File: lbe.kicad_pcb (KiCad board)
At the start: 2 copper layers, 95 parts, among them J1 Screw_Terminal_1x03, J2 IN, J3 IN, J4 IN, J5 IN, J6 IN, J7 IN, J8 IN, J9 IN, M1 BLUEPILL_STM8S103F3, U1 SN74LV1T34, U2 74HC245, U3 MCP6004, U4 MCP6004

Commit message: Layout complete
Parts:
- added J10: Screw_Terminal_1x02, Connectors_Phoenix:PhoenixContact_MC-G_02x3.81mm_Angled, F.Cu at (169.5, 62.2)
- added REF**: MountingHole_3.2mm_M3, Mounting_Holes:MountingHole_3.2mm_M3, F.Cu at (173.0, 47.0)
- added REF**: MountingHole_3.2mm_M3, Mounting_Holes:MountingHole_3.2mm_M3, F.Cu at (173.0, 98.0)
- added REF**: MountingHole_3.2mm_M3, Mounting_Holes:MountingHole_3.2mm_M3, F.Cu at (55.0, 98.0)
- added REF**: MountingHole_3.2mm_M3, Mounting_Holes:MountingHole_3.2mm_M3, F.Cu at (55.0, 47.0)
- C10: moved to F.Cu
- C5: footprint Capacitors_SMD:C_0603_HandSoldering -> footprints:Cap_electrolytic_8x10
- C9: moved to B.Cu
- M1: footprint Pin_Headers:Pin_Header_Straight_2x10_Pitch2.54mm -> footprints:BLUEPILL_STM8S103F3
- U2: value 74HC245 -> 74HC245_CUSTOM
- moved U1 56.7 mm to (155.9, 83.2)
- moved J1 56.2 mm to (169.5, 89.2)
- moved C10 54.5 mm to (156.0, 79.2), turned to 180 degrees
- moved C5 47.1 mm to (158.5, 60.8), turned to 90 degrees
- moved D2 46.4 mm to (154.2, 75.0), turned to 90 degrees
- moved C6 46.1 mm to (162.5, 81.5), turned to 180 degrees
- moved L1 46.0 mm to (162.5, 84.5)
- moved M1 45.6 mm to (139.4, 68.6), turned to 180 degrees
- moved R2 42.7 mm to (151.0, 76.5), turned to 270 degrees
- moved C4 42.2 mm to (144.0, 67.2), turned to 270 degrees
- moved D1 40.5 mm to (154.2, 70.0), turned to 270 degrees
- moved R1 35.1 mm to (151.0, 71.5), turned to 270 degrees
- moved C9 32.6 mm to (105.0, 60.0), turned to 270 degrees
- moved C3 30.2 mm to (141.5, 67.2), turned to 270 degrees
- moved C1 30.0 mm to (139.0, 67.2), turned to 270 degrees
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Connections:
- C10 pad 1: VDD -> +5V
- M1 pad 1: /EN1 -> /LED2
- M1 pad 11: /LED2 -> /EN1
- M1 pad 12: /D7 -> /D0
- M1 pad 13: /D6 -> /D1
- M1 pad 14: /D5 -> /D2
- M1 pad 15: /D4 -> /D3
- M1 pad 16: /D3 -> /D4
- M1 pad 17: /D2 -> /D5
- M1 pad 18: /D1 -> /D6
- M1 pad 19: /D0 -> /D7
- U2 pad 20: VCC -> VDD
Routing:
- net GND: track 420.1 -> 702.4 mm, vias 42 -> 90
- net VDD: track 43.0 -> 133.4 mm, vias 2 -> 5
- net +5V: track 0.00 -> 86.5 mm
- net /input_group0/Vref: track 52.6 -> 79.6 mm, vias 0 -> 4
- net /LED_OUT: track 0.00 -> 24.6 mm
- net /THR_PWM: track 0.00 -> 23.0 mm
- net /EN1: track 0.00 -> 9.45 mm
- net Net-(C6-Pad1): track 0.00 -> 9.21 mm
- net /D0: track 0.00 -> 8.55 mm
- net /D7: track 0.00 -> 8.50 mm
- net /LED2: track 0.00 -> 8.04 mm, vias 0 -> 2
- net /D1: track 0.00 -> 8.02 mm
- net /D6: track 0.00 -> 7.97 mm
- net /D2: track 0.00 -> 7.49 mm
- net /D5: track 0.00 -> 7.44 mm
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- added copper zone on B.Cu, net GND
- added copper zone on F.Cu, net GND
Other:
- board outline added: 126 x 59 mm
- net class power added: clearance 0.2, trace_width 2, via_dia 0.6, via_drill 0.4

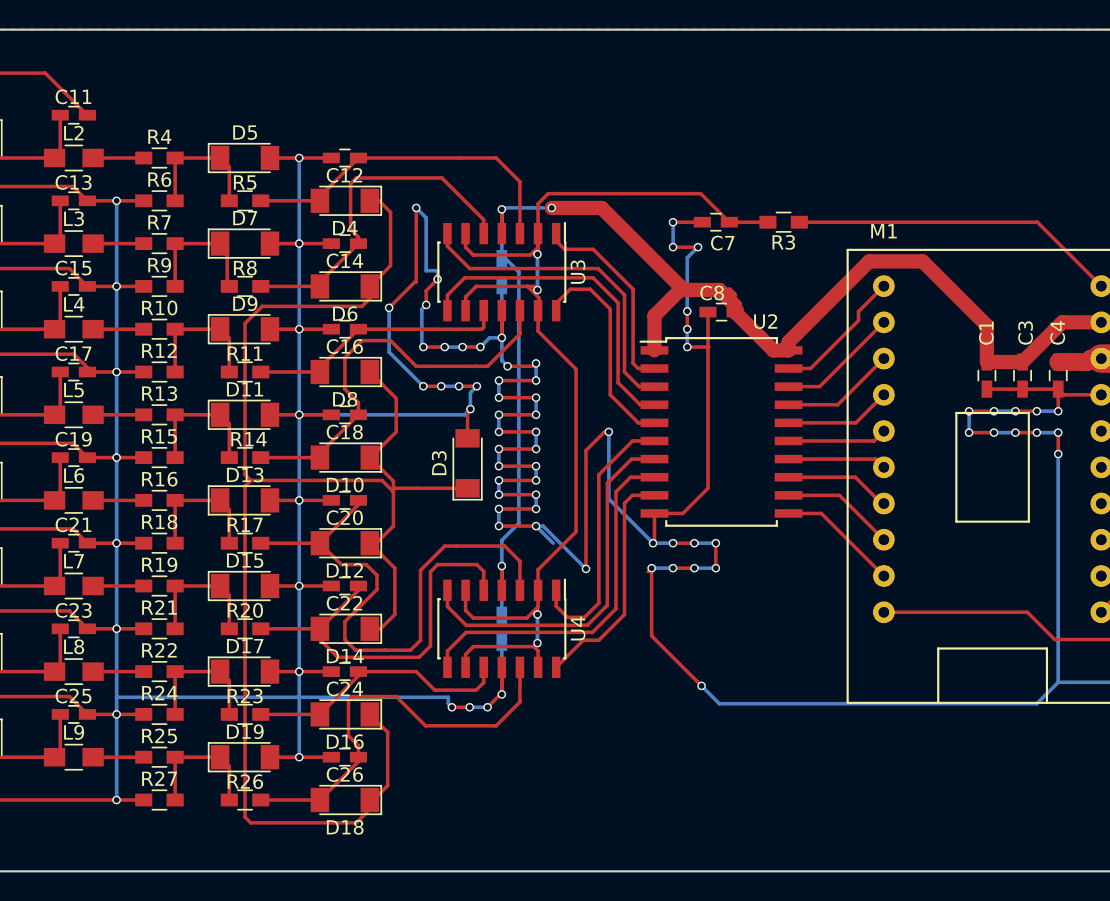
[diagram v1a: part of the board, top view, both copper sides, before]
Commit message: Add pullup option
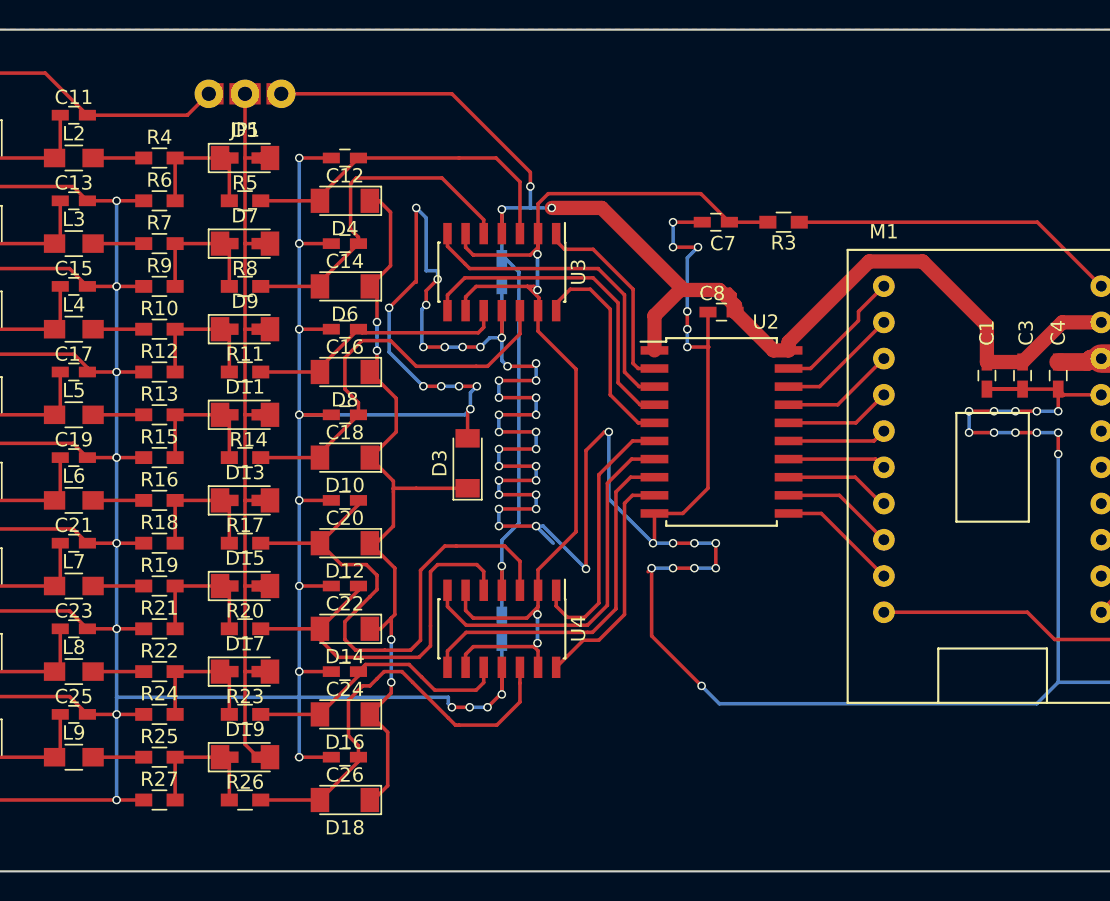
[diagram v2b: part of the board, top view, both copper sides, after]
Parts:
- added JP1: jumper_nc_no_dual, footprints:Header_with_SMD_jumper_1x3_2.54, F.Cu at (87.0, 47.5)
- D11, D13, D15, D17, D19, D5, D7, D9: footprint Diodes_SMD:D_MiniMELF_Standard -> footprints:MiniMelf_0603_combo
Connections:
- D11 pad 2: GND -> /input_group0/sheet5AD30D18/Vclamp
- D13 pad 2: GND -> /input_group0/sheet5AD30D18/Vclamp
- D15 pad 2: GND -> /input_group0/sheet5AD30D18/Vclamp
- D17 pad 2: GND -> /input_group0/sheet5AD30D18/Vclamp
- D19 pad 2: GND -> /input_group0/sheet5AD30D18/Vclamp
- D5 pad 2: GND -> /input_group0/sheet5AD30D18/Vclamp
- D7 pad 2: GND -> /input_group0/sheet5AD30D18/Vclamp
- D9 pad 2: GND -> /input_group0/sheet5AD30D18/Vclamp
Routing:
- net /input_group0/sheet5AD30D18/Vclamp: track 0.00 -> 60.0 mm
- net VCOM: track 109.1 -> 58.0 mm, vias 0 -> 4
- net VDD: track 133.4 -> 156.2 mm, vias 5 -> 6
- net GND: track 702.4 -> 695.3 mm
- net Net-(C26-Pad1): track 28.7 -> 30.1 mm
- net Net-(D7-Pad1): track 9.42 -> 10.3 mm
- net Net-(D9-Pad1): track 9.42 -> 10.1 mm
- net Net-(D19-Pad1): track 9.42 -> 10.1 mm
- net Net-(D17-Pad1): track 9.42 -> 10.1 mm
- net Net-(D15-Pad1): track 9.42 -> 10.1 mm
- net Net-(D13-Pad1): track 9.42 -> 10.1 mm
- net Net-(D11-Pad1): track 9.42 -> 10.1 mm
- net Net-(D5-Pad1): track 9.42 -> 10.1 mm

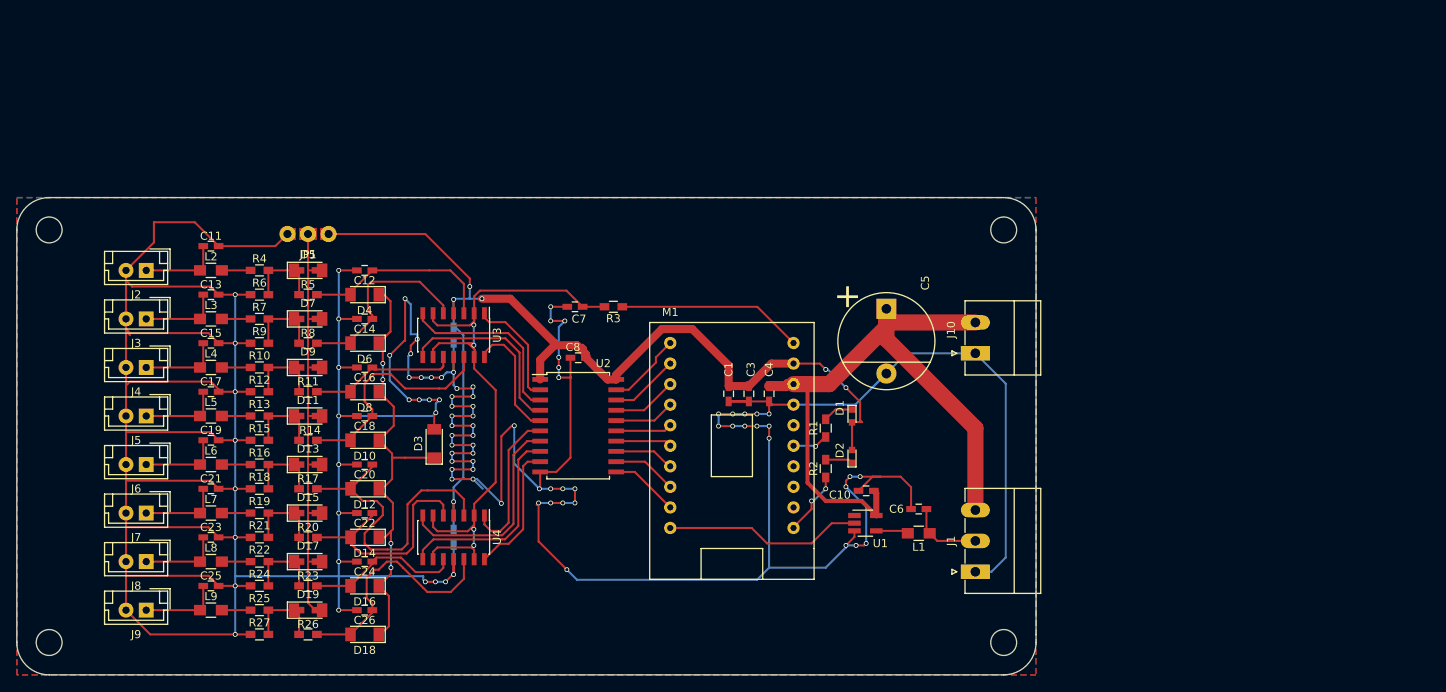
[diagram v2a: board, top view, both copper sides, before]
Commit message: 8ch version without buffer
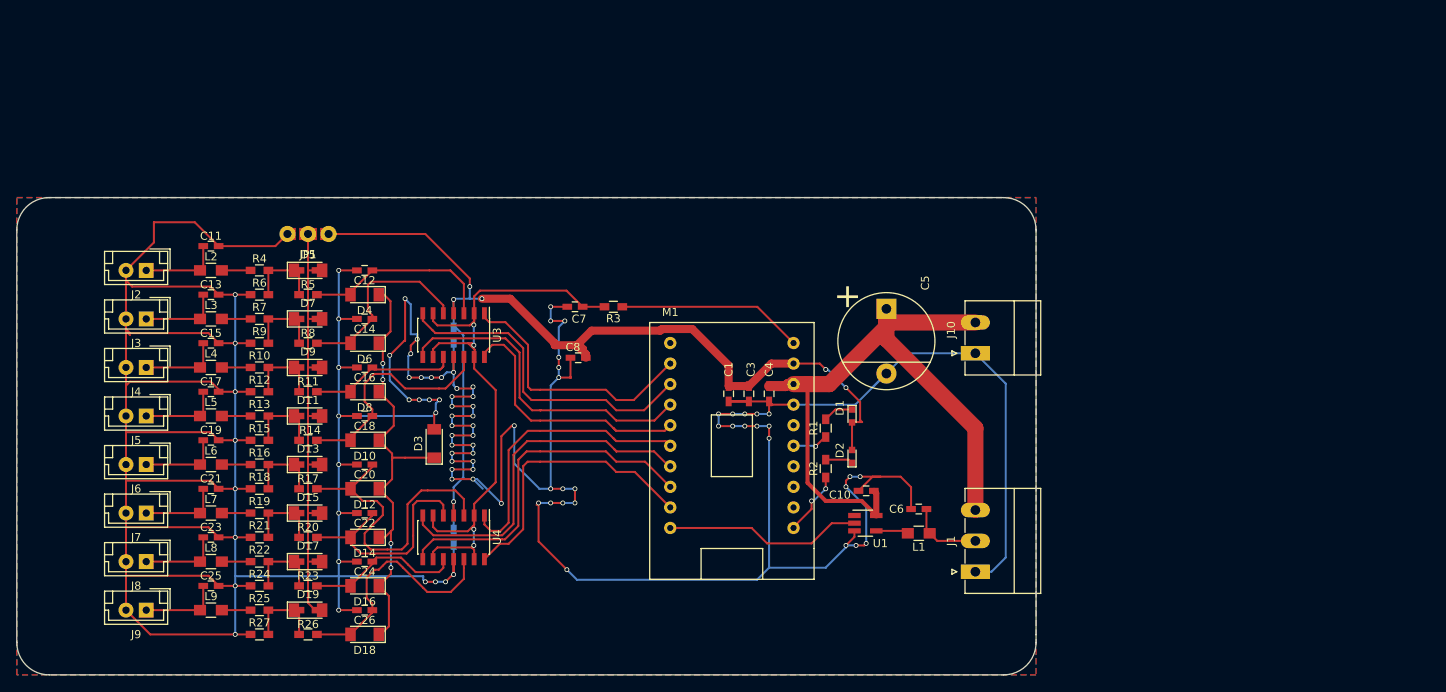
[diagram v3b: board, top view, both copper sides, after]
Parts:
- removed REF** (x4): MountingHole_3.2mm_M3, Mounting_Holes:MountingHole_3.2mm_M3
- removed U2: 74HC245_CUSTOM, Housings_SOIC:SOIC-20W_7.5x12.8mm_Pitch1.27mm
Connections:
- U3 pad 1: /input_group0/sheet5AD30D18/OUT -> /D0
- U3 pad 14: /input_group0/sheet5AD30D1B/OUT -> /D3
- U3 pad 7: /input_group0/sheet5AD30D19/OUT -> /D1
- U3 pad 8: /input_group0/sheet5AD30D1A/OUT -> /D2
- U4 pad 1: /input_group0/sheet5AD30D1C/OUT -> /D4
- U4 pad 14: /input_group0/sheet5AD30D1F/OUT -> /D7
- U4 pad 7: /input_group0/sheet5AD30D1D/OUT -> /D5
- U4 pad 8: /input_group0/sheet5AD30D1E/OUT -> /D6
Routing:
- net /D5: track 7.44 -> 43.6 mm
- net /D6: track 7.97 -> 43.4 mm
- net /D2: track 7.49 -> 40.5 mm
- net /D1: track 8.02 -> 40.6 mm
- net /D4: track 6.92 -> 35.9 mm
- net /D7: track 8.50 -> 34.9 mm
- net /input_group0/sheet5AD30D1D/OUT: track 26.0 -> 0.00 mm
- net /input_group0/sheet5AD30D1E/OUT: track 25.5 -> 0.00 mm
- net /D3: track 6.97 -> 32.4 mm
- net /D0: track 8.55 -> 32.6 mm
- net /input_group0/sheet5AD30D1A/OUT: track 23.1 -> 0.00 mm
- net /input_group0/sheet5AD30D19/OUT: track 22.6 -> 0.00 mm
- net /input_group0/sheet5AD30D1C/OUT: track 18.7 -> 0.00 mm
- net /input_group0/sheet5AD30D1F/OUT: track 16.5 -> 0.00 mm
- net /input_group0/sheet5AD30D1B/OUT: track 15.2 -> 0.00 mm
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
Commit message: Add serial header, restore holes
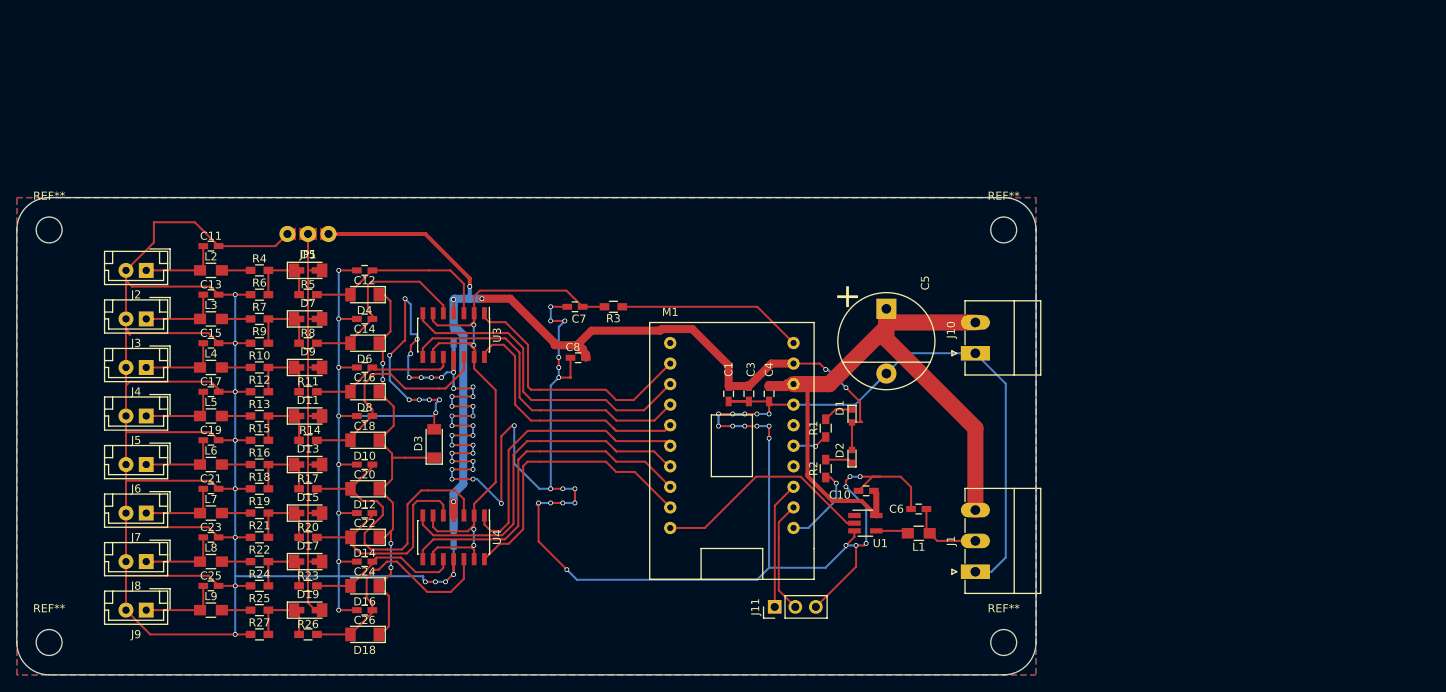
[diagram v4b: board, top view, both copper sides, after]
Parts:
- added J11: CONN_01X03, Pin_Headers:Pin_Header_Straight_1x03_Pitch2.54mm, F.Cu at (144.7, 93.6)
- added REF**: MountingHole_3.2mm_M3, Mounting_Holes:MountingHole_3.2mm_M3, F.Cu at (55.0, 47.0)
- added REF**: MountingHole_3.2mm_M3, Mounting_Holes:MountingHole_3.2mm_M3, F.Cu at (173.0, 47.0)
- added REF**: MountingHole_3.2mm_M3, Mounting_Holes:MountingHole_3.2mm_M3, F.Cu at (173.0, 98.0)
- added REF**: MountingHole_3.2mm_M3, Mounting_Holes:MountingHole_3.2mm_M3, F.Cu at (55.0, 98.0)
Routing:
- net /RX: track 0.00 -> 15.8 mm
- net /TX: track 0.00 -> 13.9 mm
- net GND: track 693.0 -> 701.1 mm
- net /LED_OUT: track 24.6 -> 27.8 mm
- net /LED2: track 8.04 -> 10.5 mm, vias 2 -> 1
